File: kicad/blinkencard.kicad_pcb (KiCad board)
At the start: 2 copper layers, 88.9 x 50.8 mm, 70 parts, among them Q1 BC847, Q2 BC847, Q3 BC847, Q4 BC847, Q5 BC847, SW1 LEFT, SW2 1, SW3 0, SW4 RIGHT, U1 ICE40UP5K-SG48ITR, U2 ESP32-WROOM-32D

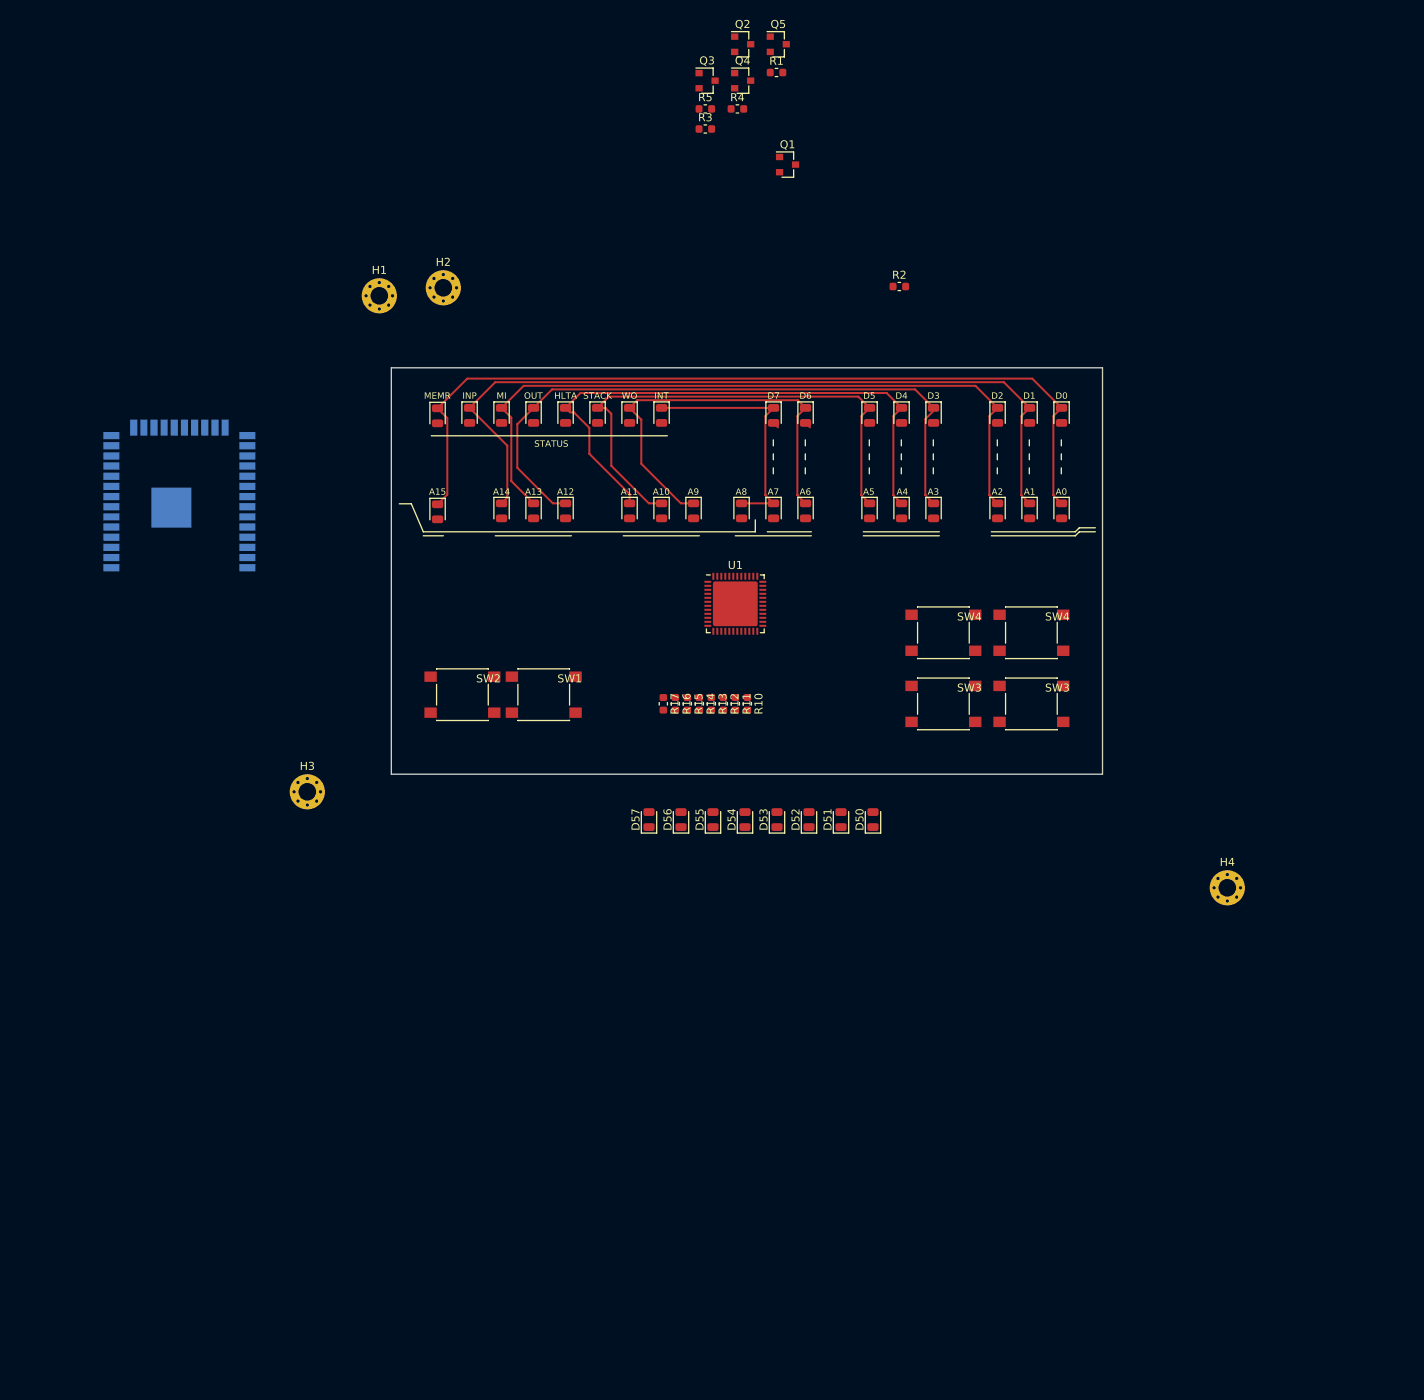
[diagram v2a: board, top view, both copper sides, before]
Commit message: Start routing LEDs. Start ESP32 integration
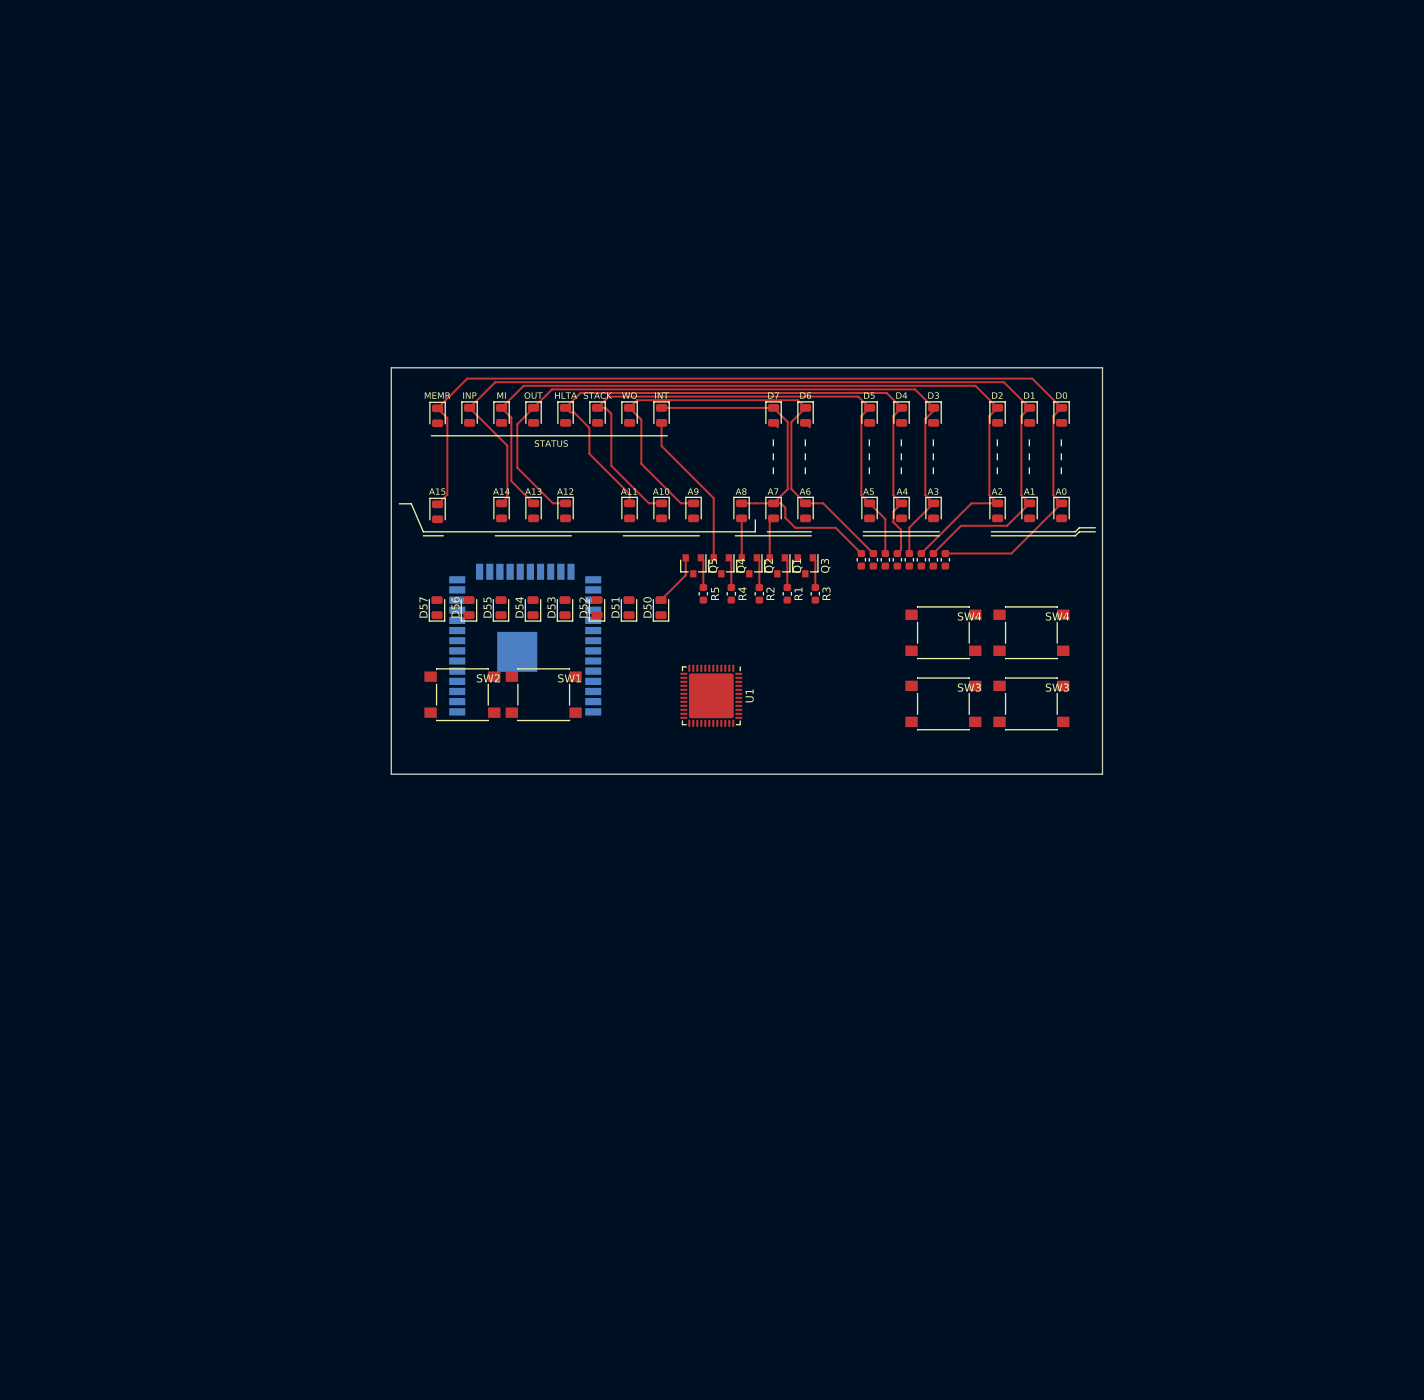
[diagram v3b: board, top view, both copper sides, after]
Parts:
- removed H1, H2, H3, H4: MountingHole_Pad, MountingHole:MountingHole_2.2mm_M2_Pad_Via
- moved Q5 66.0 mm to (37.8, 24.8), turned to 270 degrees
- moved Q2 65.2 mm to (44.8, 24.8), turned to 270 degrees
- moved R1 65.2 mm to (49.5, 28.2), turned to 270 degrees
- moved Q3 61.9 mm to (51.8, 24.8), turned to 270 degrees
- moved Q4 60.7 mm to (41.2, 24.8), turned to 270 degrees
- moved R4 60.6 mm to (42.5, 28.2), turned to 270 degrees
- moved R5 60.6 mm to (39.0, 28.2), turned to 270 degrees
- moved R3 59.7 mm to (53.0, 28.2), turned to 270 degrees
- moved Q1 50.2 mm to (48.2, 24.8), turned to 270 degrees
- moved U2 46.8 mm to (16.8, 34.8)
- moved R2 42.2 mm to (46.0, 28.2), turned to 270 degrees
- moved R17 39.6 mm to (69.2, 24.0)
- moved D50 37.5 mm to (33.7, 30.0)
- moved D51 37.5 mm to (29.7, 30.0)
- moved D52 37.5 mm to (25.7, 30.0)
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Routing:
- net Net-(D40-Pad2): track 0.00 -> 19.6 mm
- net Net-(D17-Pad1): track 106.8 -> 124.0 mm
- net Net-(D10-Pad1): track 30.8 -> 45.7 mm
- net Net-(D16-Pad1): track 99.6 -> 114.3 mm
- net Net-(D15-Pad1): track 90.7 -> 102.8 mm
- net Net-(D11-Pad1): track 51.8 -> 63.4 mm
- net Net-(D14-Pad1): track 80.9 -> 88.4 mm
- net Net-(D13-Pad1): track 71.8 -> 79.1 mm
- net Net-(D12-Pad1): track 64.7 -> 71.8 mm
- net Net-(D50-Pad2): track 0.00 -> 6.56 mm
- net Net-(D10-Pad2): track 0.00 -> 5.13 mm
- net Net-(D20-Pad2): track 0.00 -> 4.94 mm
- net Net-(Q5-Pad1): track 0.00 -> 3.91 mm
- net Net-(Q4-Pad1): track 0.00 -> 3.91 mm
- net Net-(Q3-Pad1): track 0.00 -> 3.91 mm
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
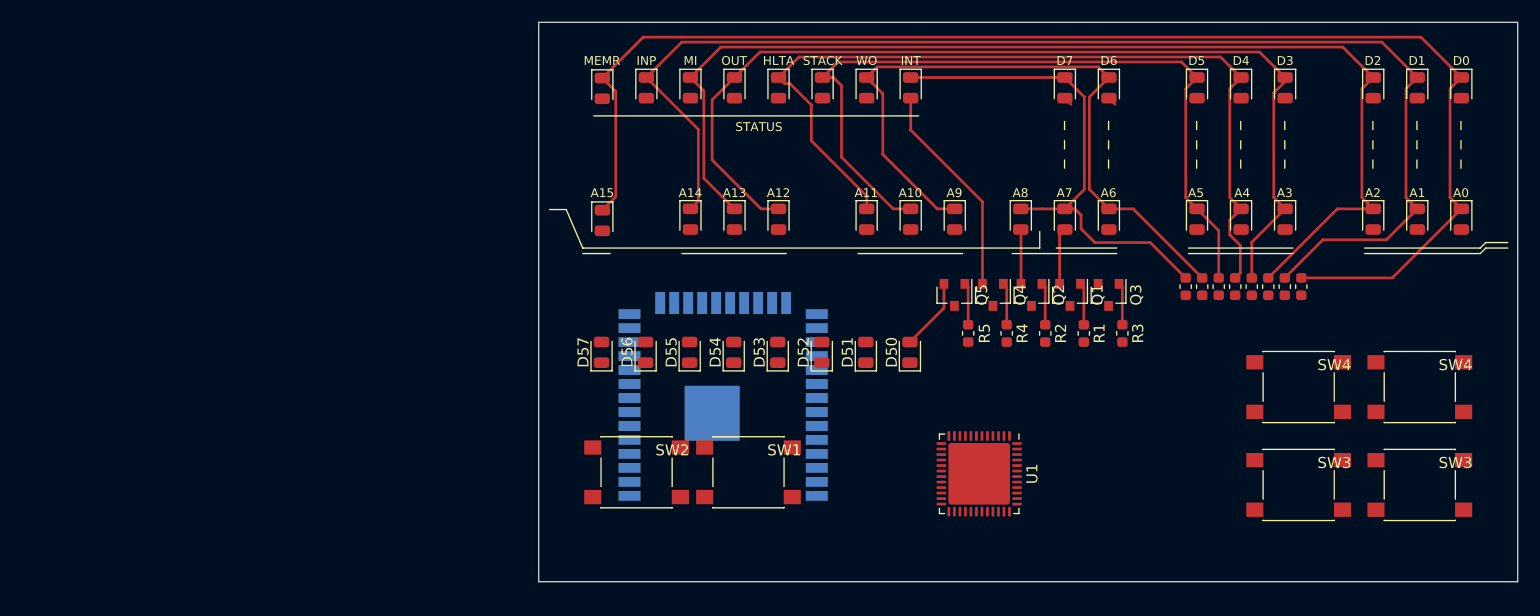
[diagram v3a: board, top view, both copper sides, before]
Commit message: Decided to use bottom-firing LEDs. Need to reassign LED refdes
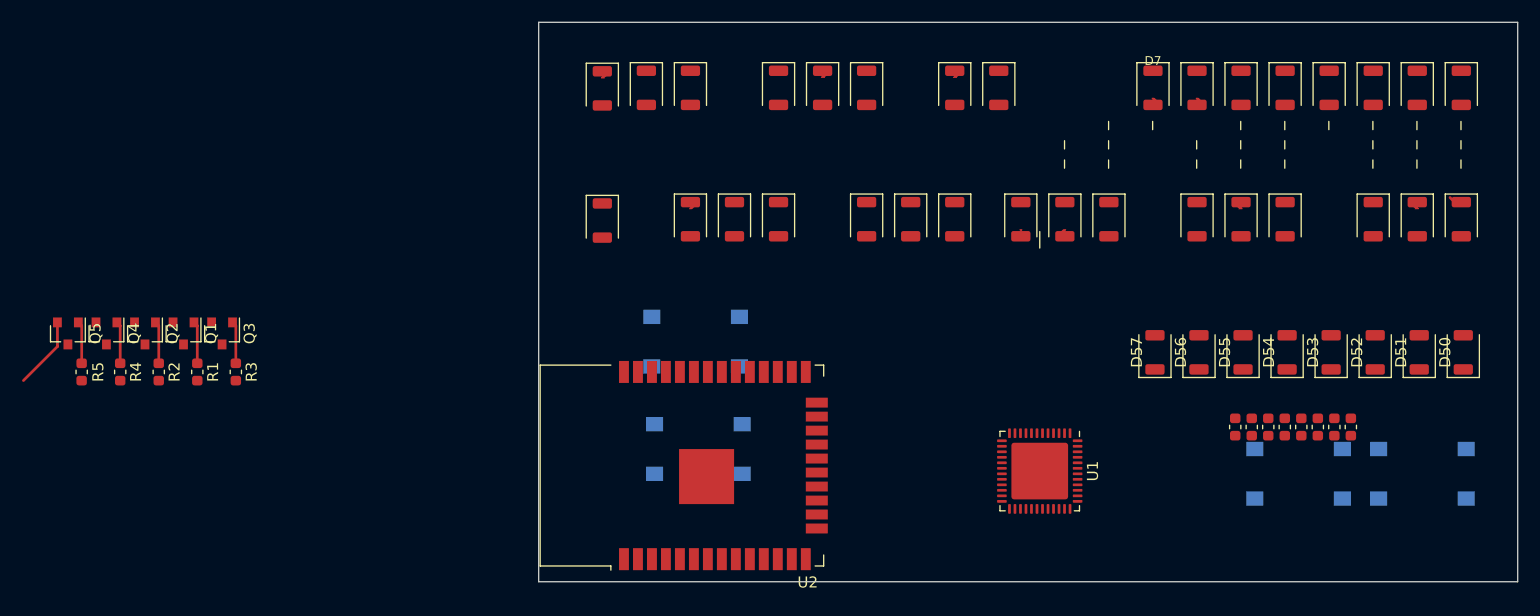
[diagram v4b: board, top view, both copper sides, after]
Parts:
- removed SW1: LEFT, Button_Switch_SMD:SW_SPST_PTS645
- removed SW2: 1, Button_Switch_SMD:SW_SPST_PTS645
- removed SW3 (x2): 0, Button_Switch_SMD:SW_SPST_PTS645
- removed SW4 (x2): RIGHT, Button_Switch_SMD:SW_SPST_PTS645
- added REF**: SW_SPST_PTS645, Button_Switch_SMD:SW_SPST_PTS645, B.Cu at (14.5, 38.8)
- added REF**: SW_SPST_PTS645, Button_Switch_SMD:SW_SPST_PTS645, B.Cu at (14.2, 29.0)
- added REF**: SW_SPST_PTS645, Button_Switch_SMD:SW_SPST_PTS645, B.Cu at (69.0, 41.0)
- added REF**: SW_SPST_PTS645, Button_Switch_SMD:SW_SPST_PTS645, B.Cu at (80.2, 41.0)
- D10, D11, D12, D13, D14, D15, D16, D17, D20, D21, D22, D23, D24, D25, D26, D27, D30, D31, D32, D33, D34, D35, D36, D37, D40, D41, D42, D43, D44, D45, D46, D47, D50, D51, D52, D53, D54, D55, D56, D57: footprint LED_SMD:LED_0805_2012Metric -> LED_SMD:LED_1206_3216Metric_ReverseMount_Hole1.8x2.4mm
- U1: footprint Package_DFN_QFN:QFN-48-1EP_7x7mm_P0.5mm_EP5.6x5.6mm -> Package_DFN_QFN:QFN-48-1EP_7x7mm_P0.5mm_EP5.15x5.15mm
- U2: moved to F.Cu
- moved Q1 80.6 mm to (-32.2, 28.2)
- moved Q2 80.6 mm to (-35.8, 28.2)
- moved Q3 80.6 mm to (-28.8, 28.2)
- moved Q4 80.6 mm to (-39.2, 28.2)
- moved Q5 80.6 mm to (-42.8, 28.2)
- moved R1 80.6 mm to (-31.0, 31.8)
- moved R2 80.6 mm to (-34.5, 31.8)
- moved R3 80.6 mm to (-27.5, 31.8)
- moved R4 80.6 mm to (-38.0, 31.8)
- moved R5 80.6 mm to (-41.5, 31.8)
- moved D55 50.2 mm to (64.0, 30.0)
- moved D56 50.2 mm to (60.0, 30.0)
- moved D57 50.2 mm to (56.0, 30.0)
- moved D50 50.2 mm to (84.0, 30.0)
- moved D51 50.2 mm to (80.0, 30.0)
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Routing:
- net Net-(D17-Pad1): track 124.0 -> 2.24 mm
- net Net-(D16-Pad1): track 114.3 -> 2.59 mm
- net Net-(D15-Pad1): track 102.8 -> 0.00 mm
- net Net-(D14-Pad1): track 88.4 -> 0.00 mm
- net Net-(D13-Pad1): track 79.1 -> 3.15 mm
- net Net-(D12-Pad1): track 71.8 -> 0.00 mm
- net Net-(D11-Pad1): track 63.4 -> 1.57 mm
- net Net-(D10-Pad1): track 45.7 -> 0.00 mm
- net Net-(D40-Pad2): track 19.6 -> 0.00 mm
- net Net-(D20-Pad2): track 4.94 -> 0.03 mm
- net Net-(D10-Pad2): track 5.13 -> 0.68 mm
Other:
- copper layers 2 -> 4

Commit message: More flat front panel work
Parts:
- moved D25 10.0 mm to (65.8, 17.9)
- moved D26 10.0 mm to (69.8, 17.9)
- moved D22 8.00 mm to (51.8, 17.9)
- moved D23 8.00 mm to (55.8, 17.9)
- moved D27 8.00 mm to (75.8, 17.9)
- moved D14 6.00 mm to (23.8, 17.9)
- moved D15 6.00 mm to (27.8, 17.9)
- moved D17 6.00 mm to (37.8, 17.9)
- moved D20 6.00 mm to (41.8, 17.9)
- moved D24 6.00 mm to (61.8, 17.9)
- moved D12 4.00 mm to (13.8, 17.9)
- moved D11 4.00 mm to (9.78, 17.9)
- moved D16 4.00 mm to (33.8, 17.9)
- moved D21 4.00 mm to (47.8, 17.9)
- moved D36 4.00 mm to (33.8, 5.95)
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- renumbered D27 to D10, D26 to D11, D25 to D12, D24 to D13, D23 to D14, D22 to D15, D21 to D16, D20 to D17, D10 to D20, D11 to D21, D12 to D22, D13 to D23, D14 to D24, D15 to D25, D16 to D26, D17 to D27, D47 to D30, D46 to D31, D45 to D32, D44 to D33, D43 to D34, D42 to D35, D41 to D36, D40 to D37, D30 to D40, D31 to D41, D32 to D42, D33 to D43, D34 to D44, D35 to D45, D36 to D46, D37 to D47, D57 to D50, D56 to D51, D55 to D52, D54 to D53, D53 to D54, D52 to D55, D51 to D56, D50 to D57
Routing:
- net Net-(D17-Pad1): track 2.24 -> 1.57 mm
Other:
- board text added: "Addr"
- board text added: "CLR"
- board text added: "DEP"
- board text added: "DEPN"
- board text added: "Data"
- board text added: "EDIT"
- board text added: "EX"
- board text added: "EXN"
- board text added: "IDLE"
- board text added: "L"
- board text added: "MODE SW"
- board text added: "R"
- board text added: "RST"
- board text added: "SENSE SW."
- board text added: "SET0"
- board text added: "SET1"
- board text added: "SS"
